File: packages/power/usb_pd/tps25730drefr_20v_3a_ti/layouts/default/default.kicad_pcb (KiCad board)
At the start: 2 copper layers, 9 parts

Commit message: Finish removing net-name overrides from reusable packages
This completes the package-level override cleanup by deleting the remaining
`override_net_name` assignments from the library's reusable package modules and
rebuilding their checked-in layouts so generated net metadata matches source.
The package interfaces stay the same; only the forced net naming was removed so
these modules compose cleanly when imported into downstream designs.

Constraint: The library must stay reusable and avoid imposed internal net names leaking into consuming designs
Constraint: Each changed package must still verify with the repo's Atopile workflow after layout regeneration
Rejected: Stop after the battery frontend cleanup | leaves the same composition hazard in other packages
Rejected: Remove override lines without rebuilding layouts | would leave stale generated PCB net names checked into the repo
Confidence: high
Scope-risk: moderate
Reversibility: clean
Directive: Do not reintroduce `override_net_name` in reusable package modules unless a package is intentionally design-specific
Tested: `uv tool run --from atopile==0.15.4 ato --non-interactive build` in each affected package directory (stm32g0b1kbu6_st, mcp2518fdt_e_sl_microchip, tcan3413ddfr_ti, raspberry_pi_hat_socket_zhouri, tps56637rpar_5v1_5a_ti, tps62933drlr_3v3_ti, bq25756rrvr_4s_2a_ti, tps2121ruxr_20v_4a_ti, tps25730drefr_20v_3a_ti)
Not-tested: Downstream consumer projects that may have been depending on the old forced net names in generated layouts
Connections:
- net 3V3 renamed hv
- net CC1 renamed cc1-1
- net CC2 renamed cc2-1
- net GND renamed lv
- net LDO_1V5 renamed controller-1
- net LDO_3V3 renamed adc_limit_top-1
- net PD_LIMIT_SEL renamed 1
- net SINK_VBUS renamed sink_vbus-hv
- net USB_VBUS renamed usb_vbus-hv
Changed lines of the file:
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@@
 		)
 	)
-	(net 2 "CC1")
+	(net 2 "cc1-1")
 	(net 3 "DBG_ACC")
 	(net 4 "PLUG_FLIP")
 	(net 5 "nSINK_EN")
-	(net 6 "USB_VBUS")
-	(net 7 "CC2")
+	(net 6 "usb_vbus-hv")
+	(net 7 "cc2-1")
 	(net 8 "PLUG_EVENT")
-	(net 9 "3V3")
+	(net 9 "hv")
 	(net 10 "CAP_MIS")
-	(net 11 "PD_LIMIT_SEL")
+	(net 11 "1")
 	(net 12 "SDA")
 	(net 13 "SCL")
-	(net 14 "LDO_1V5")
-	(net 15 "LDO_3V3")
-	(net 16 "SINK_VBUS")
-	(net 17 "GND")
+	(net 14 "controller-1")
+	(net 15 "adc_limit_top-1")
+	(net 16 "sink_vbus-hv")
+	(net 17 "lv")
 	(footprint "TEXAS_INSTRUMENTS_TPS25730DREFR:QFN-38_L6.0-W4.0-P0.40-TL-EP_RJK"
 		(layer "F.Cu")
@@
 			(size 0.6 0.2)
 			(layers "F.Cu" "F.Paste" "F.Mask")
-			(net 15 "LDO_3V3")
+			(net 15 "adc_limit_top-1")
 		)
 		(pad "2" smd rect
@@
 			(size 0.6 0.2)
 			(layers "F.Cu" "F.Paste" "F.Mask")
-			(net 17 "GND")
+			(net 17 "lv")
 		)
 		(pad "3" smd rect
@@
 			(size 0.6 0.2)
 			(layers "F.Cu" "F.Paste" "F.Mask")
-			(net 15 "LDO_3V3")
+			(net 15 "adc_limit_top-1")
 		)
 		(pad "4" smd rect
@@
 			(size 0.6 0.2)
 			(layers "F.Cu" "F.Paste" "F.Mask")
-			(net 14 "LDO_1V5")
+			(net 14 "controller-1")
 		)
 		(pad "5" smd rect
@@
 			(size 0.6 0.2)
 			(layers "F.Cu" "F.Paste" "F.Mask")
-			(net 17 "GND")
+			(net 17 "lv")
 		)
 		(pad "6" smd rect
@@
 			(size 0.2 0.6)
 			(layers "F.Cu" "F.Paste" "F.Mask")
-			(net 11 "PD_LIMIT_SEL")
+			(net 11 "1")
 		)
 		(pad "8" smd rect
@@
 			(size 0.2 0.6)
 			(layers "F.Cu" "F.Paste" "F.Mask")
-			(net 17 "GND")
+			(net 17 "lv")
 		)
 		(pad "12" smd rect
@@
 			(size 0.2 0.6)
 			(layers "F.Cu" "F.Paste" "F.Mask")
-			(net 17 "GND")
+			(net 17 "lv")
 		)
 		(pad "13" smd rect
@@
 			(size 0.2 0.6)
 			(layers "F.Cu" "F.Paste" "F.Mask")
-			(net 17 "GND")
+			(net 17 "lv")
 		)
 		(pad "15" smd rect
@@
 			(size 0.2 0.6)
 			(layers "F.Cu" "F.Paste" "F.Mask")
-			(net 6 "USB_VBUS")
+			(net 6 "usb_vbus-hv")
 		)
 		(pad "16" smd rect
@@
 			(size 0.2 0.6)
 			(layers "F.Cu" "F.Paste" "F.Mask")
-			(net 17 "GND")
+			(net 17 "lv")
 		)
 		(pad "17" smd rect
@@
 			(size 0.2 0.6)
 			(layers "F.Cu" "F.Paste" "F.Mask")
-			(net 17 "GND")
+			(net 17 "lv")
 		)
 		(pad "18" smd rect
@@
 			(size 0.2 0.6)
 			(layers "F.Cu" "F.Paste" "F.Mask")
-			(net 15 "LDO_3V3")
+			(net 15 "adc_limit_top-1")
 		)
 		(pad "19" smd rect
@@
 			(size 0.6 0.22)
 			(layers "F.Cu" "F.Paste" "F.Mask")
-			(net 16 "SINK_VBUS")
+			(net 16 "sink_vbus-hv")
 		)
 		(pad "21" smd rect
@@
 			(size 0.6 0.22)
 			(layers "F.Cu" "F.Paste" "F.Mask")
-			(net 16 "SINK_VBUS")
+			(net 16 "sink_vbus-hv")
 		)
 		(pad "22" smd rect
@@
 			(size 0.6 0.22)
 			(layers "F.Cu" "F.Paste" "F.Mask")
-			(net 16 "SINK_VBUS")
+			(net 16 "sink_vbus-hv")
 		)
 		(pad "23" smd rect
@@
 			(size 0.6 0.22)
 			(layers "F.Cu" "F.Paste" "F.Mask")
-			(net 6 "USB_VBUS")
+			(net 6 "usb_vbus-hv")
 		)
 		(pad "24" smd rect
@@
 			(size 0.6 0.22)
 			(layers "F.Cu" "F.Paste" "F.Mask")
-			(net 6 "USB_VBUS")
+			(net 6 "usb_vbus-hv")
 		)
 		(pad "25" smd rect
@@
 			(size 0.6 0.22)
 			(layers "F.Cu" "F.Paste" "F.Mask")
-			(net 6 "USB_VBUS")
+			(net 6 "usb_vbus-hv")
 		)
 		(pad "26" smd rect
@@
 			(size 0.2 0.6)
 			(layers "F.Cu" "F.Paste" "F.Mask")
-			(net 17 "GND")
+			(net 17 "lv")
 		)
 		(pad "27" smd rect
@@
 			(size 0.2 0.6)
 			(layers "F.Cu" "F.Paste" "F.Mask")
-			(net 17 "GND")
+			(net 17 "lv")
 		)
 		(pad "28" smd rect
@@
 			(size 0.2 0.6)
 			(layers "F.Cu" "F.Paste" "F.Mask")
-			(net 2 "CC1")
+			(net 2 "cc1-1")
 		)
 		(pad "29" smd rect
@@
 			(size 0.2 0.6)
 			(layers "F.Cu" "F.Paste" "F.Mask")
-			(net 7 "CC2")
+			(net 7 "cc2-1")
 		)
 		(pad "30" smd rect
@@
 			(size 0.2 0.6)
 			(layers "F.Cu" "F.Paste" "F.Mask")
-			(net 6 "USB_VBUS")
+			(net 6 "usb_vbus-hv")
 		)
 		(pad "31" smd rect
@@
 			(size 0.2 0.6)
 			(layers "F.Cu" "F.Paste" "F.Mask")
-			(net 17 "GND")
+			(net 17 "lv")
 		)
 		(pad "32" smd rect
@@
 			(size 0.2 0.6)
 			(layers "F.Cu" "F.Paste" "F.Mask")
-			(net 6 "USB_VBUS")
+			(net 6 "usb_vbus-hv")
 		)
 		(pad "33" smd rect
@@
 			(size 0.2 0.6)
 			(layers "F.Cu" "F.Paste" "F.Mask")
-			(net 6 "USB_VBUS")
+			(net 6 "usb_vbus-hv")
 		)
 		(pad "34" smd rect
@@
 			(size 0.2 0.6)
 			(layers "F.Cu" "F.Paste" "F.Mask")
-			(net 17 "GND")
+			(net 17 "lv")
 		)
 		(pad "35" smd rect
@@
 			(size 0.2 0.6)
 			(layers "F.Cu" "F.Paste" "F.Mask")
-			(net 17 "GND")
+			(net 17 "lv")
 		)
 		(pad "36" smd rect
@@
 			(size 0.2 0.6)
 			(layers "F.Cu" "F.Paste" "F.Mask")
-			(net 17 "GND")
+			(net 17 "lv")
 		)
 		(pad "37" smd rect
@@
 			(size 0.2 0.6)
 			(layers "F.Cu" "F.Paste" "F.Mask")
-			(net 9 "3V3")
+			(net 9 "hv")
 		)
 		(pad "39" smd rect
@@
 			(size 2.65 2.65)
 			(layers "F.Cu" "F.Paste" "F.Mask")
-			(net 17 "GND")
+			(net 17 "lv")
 		)
 		(pad "35" smd custom
@@
 			(size 0.01 0.01)
 			(layers "F.Cu" "F.Paste" "F.Mask")
-			(net 17 "GND")
+			(net 17 "lv")
 			(primitives
 				(gr_poly
@@
 			(size 0.01 0.01)
 			(layers "F.Cu" "F.Paste" "F.Mask")
-			(net 6 "USB_VBUS")
+			(net 6 "usb_vbus-hv")
 			(primitives
 				(gr_poly
@@
 			(size 0.01 0.01)
 			(layers "F.Cu" "F.Paste" "F.Mask")
-			(net 6 "USB_VBUS")
+			(net 6 "usb_vbus-hv")
 			(primitives
 				(gr_poly
@@
 			(size 0.01 0.01)
 			(layers "F.Cu" "F.Paste" "F.Mask")
-			(net 16 "SINK_VBUS")
+			(net 16 "sink_vbus-hv")
 			(primitives
 				(gr_poly
@@
 			(size 1.53 2.65)
 			(layers "F.Cu" "F.Paste" "F.Mask")
-			(net 6 "USB_VBUS")
+			(net 6 "usb_vbus-hv")
 		)
 		(embedded_fonts no)
@@
 			(size 0.57 0.54)
 			(layers "F.Cu" "F.Paste" "F.Mask")
-			(net 17 "GND")
+			(net 17 "lv")
 		)
 		(pad "1" smd rect
@@
 			(size 0.57 0.54)
 			(layers "F.Cu" "F.Paste" "F.Mask")
-			(net 11 "PD_LIMIT_SEL")
+			(net 11 "1")
 		)
 		(embedded_fonts no)
@@
 			(size 0.57 0.54)
 			(layers "F.Cu" "F.Paste" "F.Mask")
-			(net 11 "PD_LIMIT_SEL")
+			(net 11 "1")
 		)
 		(pad "1" smd rect
@@
 			(size 0.57 0.54)
 			(layers "F.Cu" "F.Paste" "F.Mask")
-			(net 15 "LDO_3V3")
+			(net 15 "adc_limit_top-1")
 		)
 		(embedded_fonts no)
@@
 			(size 0.5 0.54)
 			(layers "F.Cu" "F.Paste" "F.Mask")
-			(net 17 "GND")
+			(net 17 "lv")
 		)
 		(pad "1" smd rect
@@
 			(size 0.5 0.54)
 			(layers "F.Cu" "F.Paste" "F.Mask")
-			(net 2 "CC1")
+			(net 2 "cc1-1")
 		)
 		(embedded_fonts no)
@@
 			(size 0.5 0.54)
 			(layers "F.Cu" "F.Paste" "F.Mask")
-			(net 17 "GND")
+			(net 17 "lv")
 		)
 		(pad "1" smd rect
@@
 			(size 0.5 0.54)
 			(layers "F.Cu" "F.Paste" "F.Mask")
-			(net 7 "CC2")
+			(net 7 "cc2-1")
 		)
 		(embedded_fonts no)
@@
 			(size 0.5 0.54)
 			(layers "F.Cu" "F.Paste" "F.Mask")
-			(net 17 "GND")
+			(net 17 "lv")
 		)
 		(pad "1" smd rect
@@
 			(size 0.5 0.54)
 			(layers "F.Cu" "F.Paste" "F.Mask")
-			(net 14 "LDO_1V5")
+			(net 14 "controller-1")
 		)
 		(embedded_fonts no)
@@
 			(size 0.8 0.9)
 			(layers "F.Cu" "F.Paste" "F.Mask")
-			(net 17 "GND")
+			(net 17 "lv")
 		)
 		(pad "1" smd rect
@@
 			(size 0.8 0.9)
 			(layers "F.Cu" "F.Paste" "F.Mask")
-			(net 15 "LDO_3V3")
+			(net 15 "adc_limit_top-1")
 		)
 		(embedded_fonts no)
@@
 			(size 0.8 0.9)
 			(layers "F.Cu" "F.Paste" "F.Mask")
-			(net 17 "GND")
+			(net 17 "lv")
 		)
 		(pad "1" smd rect
@@
 			(size 0.8 0.9)
 			(layers "F.Cu" "F.Paste" "F.Mask")
-			(net 9 "3V3")
+			(net 9 "hv")
 		)
 		(embedded_fonts no)
@@
 			(size 0.8 0.9)
 			(layers "F.Cu" "F.Paste" "F.Mask")
-			(net 17 "GND")
+			(net 17 "lv")
 		)
 		(pad "1" smd rect
@@
 			(size 0.8 0.9)
 			(layers "F.Cu" "F.Paste" "F.Mask")
-			(net 6 "USB_VBUS")
+			(net 6 "usb_vbus-hv")
 		)
 		(embedded_fonts no)

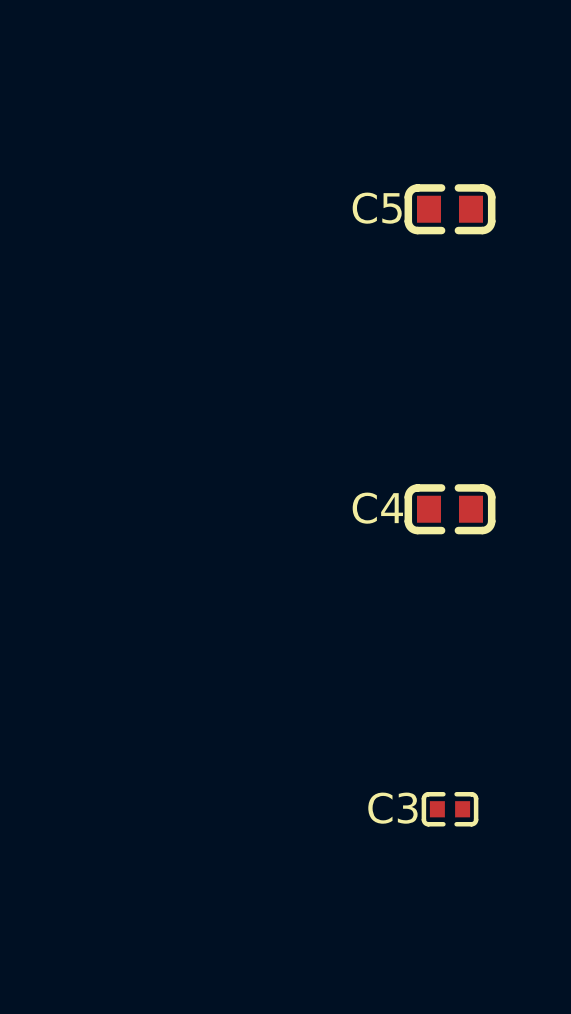
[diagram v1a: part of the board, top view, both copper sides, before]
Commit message: 22uF cap update, TPS56637 update
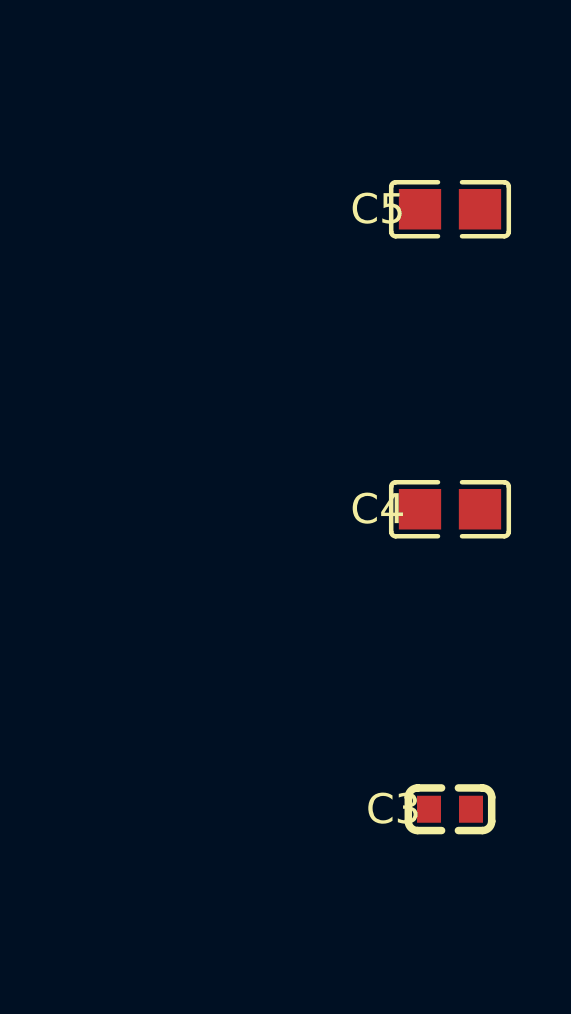
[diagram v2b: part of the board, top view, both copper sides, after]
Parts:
- C3: footprint Murata_Electronics_GRM155R61A475KEAAD:C0402 -> Murata_Electronics_GRM188R61E475KE11D:C0603
- C4, C5: footprint Murata_Electronics_GRM188R61A106KE69D:C0603 -> Murata_Electronics_GRM21BR61H106KE43L:C0805

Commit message: wip
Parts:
- moved C7 152.8 mm to (41.3, 29.6)
- moved C5 130.1 mm to (27.7, 28.9), turned to 180 degrees
- moved C4 122.3 mm to (27.8, 31.0), turned to 180 degrees
- moved C3 114.5 mm to (27.9, 33.1), turned to 180 degrees
- moved C2 83.0 mm to (34.3, 29.4), turned to 180 degrees
- moved C1 73.7 mm to (36.0, 29.0)
- moved R4 69.6 mm to (30.6, 36.5)
- moved R3 60.9 mm to (32.8, 36.5)
- moved U1 46.9 mm to (33.6, 32.7)
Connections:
- U1 pad 15: usb_vbus-hv -> DRAIN
- U1 pad 30: usb_vbus-hv -> DRAIN
- U1 pad 40: usb_vbus-hv -> DRAIN

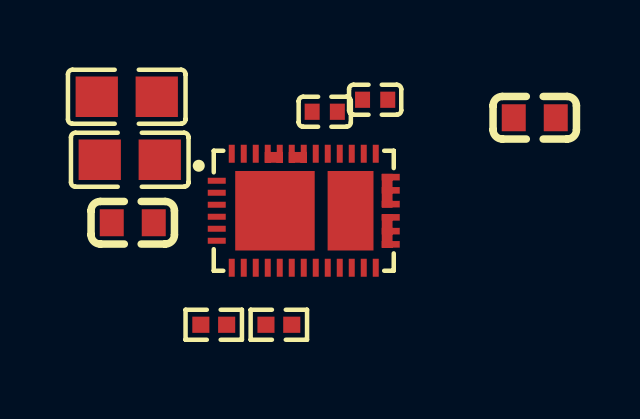
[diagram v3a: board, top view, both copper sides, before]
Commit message: tps25730 layout
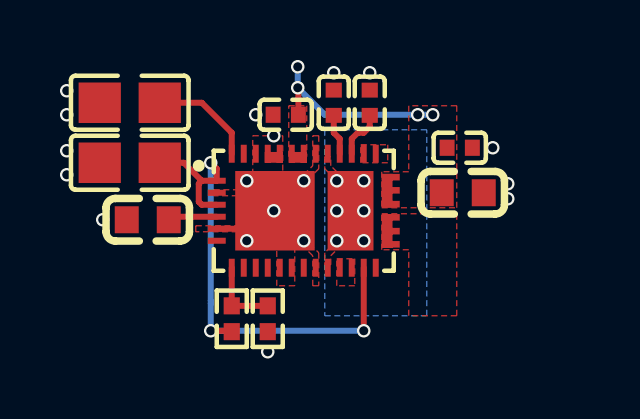
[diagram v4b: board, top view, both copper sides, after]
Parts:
- added C6: , Murata_Electronics_GRM155R71H104KE14D:C0402, F.Cu at (38.8, 30.6)
- added C8: , Murata_Electronics_GRM155R71H104KE14D:C0402, F.Cu at (33.0, 29.5)
- moved C7 3.47 mm to (38.9, 32.1)
- moved R4 0.63 mm to (31.2, 36.3), turned to 90 degrees
- moved C3 0.51 mm to (28.4, 33.0)
- moved C2 0.42 mm to (34.6, 29.1), turned to 90 degrees
- moved R3 0.42 mm to (32.4, 36.3), turned to -90 degrees
- moved C5 0.22 mm to (27.8, 29.1)
- moved C1 0.21 mm to (35.8, 29.1), turned to 90 degrees
- moved C4 0.10 mm to (27.8, 31.1)
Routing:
- net adc_limit_top-1: track 0.00 -> 17.7 mm, vias 0 -> 3
- net usb_vbus-hv: track 0.00 -> 6.48 mm, vias 0 -> 4
- net hv: track 0.00 -> 3.51 mm
- net 1: track 0.00 -> 2.47 mm
- net lv: track 0.00 -> 2.19 mm, vias 0 -> 18
- net cc1-1: track 0.00 -> 1.65 mm
- net controller-1: track 0.00 -> 1.64 mm
- net cc2-1: track 0.00 -> 1.36 mm
- net DRAIN: vias 0 -> 6
- added copper zone on B.Cu, net DRAIN
- added copper zone on F.Cu, net DRAIN
- added copper zone on F.Cu, net lv
- added copper zone on F.Cu, net sink_vbus-hv
- added copper zone on F.Cu, net usb_vbus-hv
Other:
- copper layers 2 -> 4
